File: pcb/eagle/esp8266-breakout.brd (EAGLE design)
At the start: 23.4 x 40 mm, 12 parts, among them IC1 ESP-12E/F, X1 JST-XH-11-PIN-ROUND-PAD, X2 JST-XH-11-PIN-ROUND-PAD

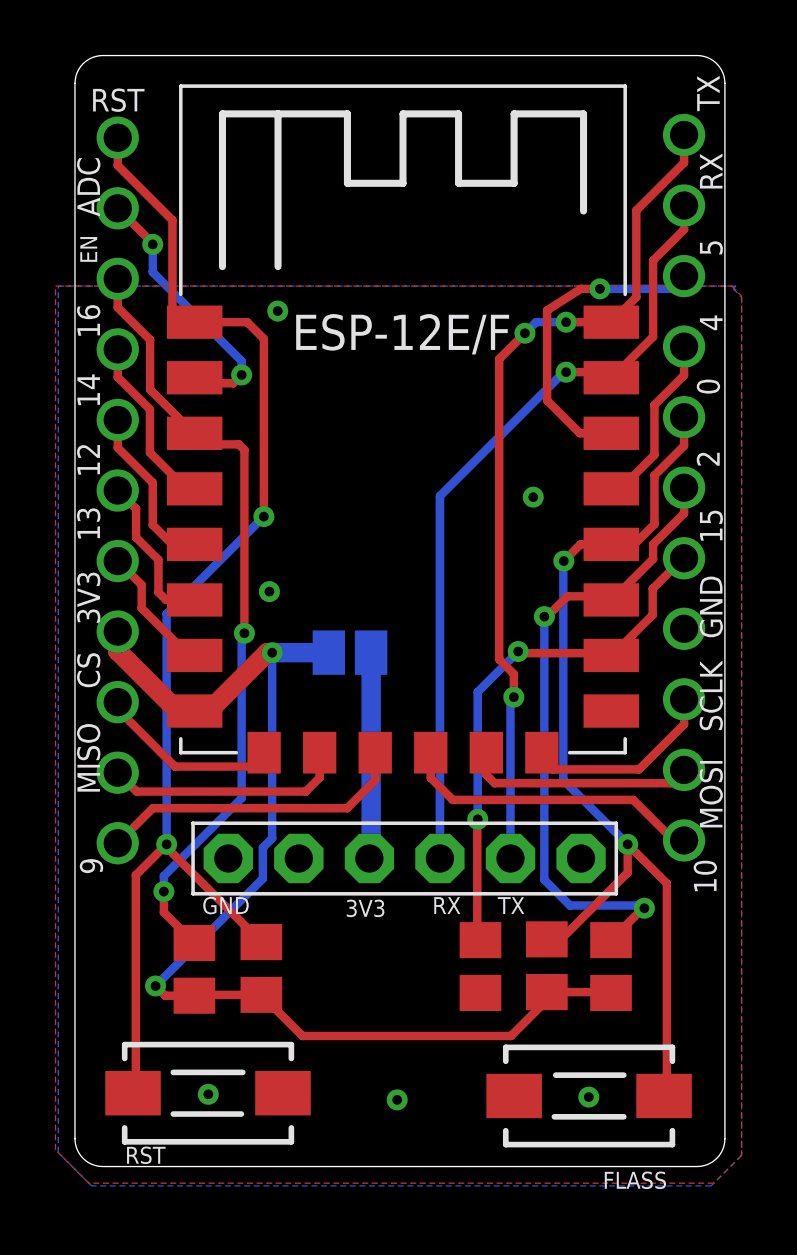
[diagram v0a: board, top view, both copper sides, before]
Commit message: Remove BUs, Rev 1.1 Completed (TODO recheck)
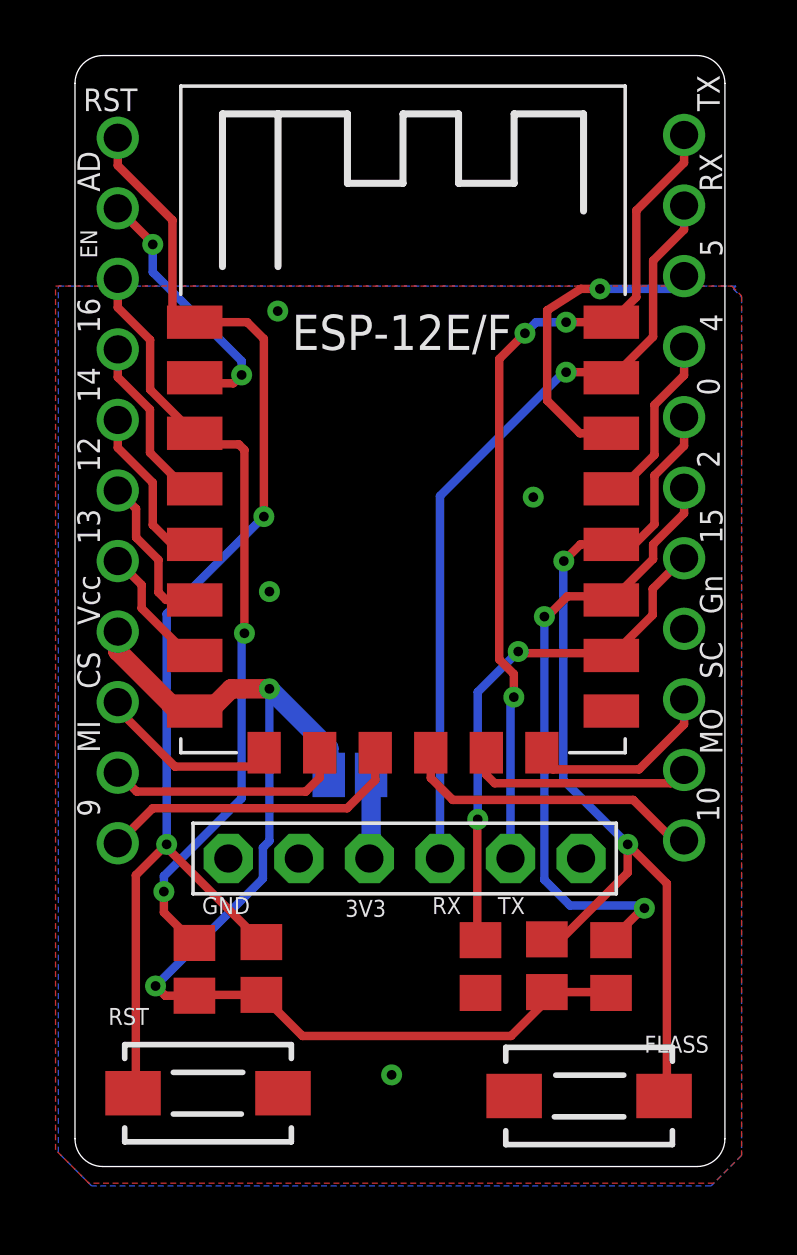
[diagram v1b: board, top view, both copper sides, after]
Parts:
- moved SJ1 4.40 mm to (9.90, 14.1)
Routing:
- net N$1: track 7.44 -> 3.04 mm
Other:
- board text added: "AD"
- board text added: "Gn"
- board text added: "MI"
- board text added: "MO"
- board text added: "SC"
- board text added: "Vcc"
- board text removed: "ADC"
- board text removed: "MISO"
- board text removed: "MOSI"
- board text removed: "SCLK"
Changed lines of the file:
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@@
 <wire x1="23.4" y1="1" x2="23.4" y2="39" width="0" layer="20"/>
 <wire x1="22.4" y1="40" x2="1" y2="40" width="0" layer="20"/>
-<text x="1.8" y="0.1" size="0.6096" layer="21">RST</text>
-<text x="19" y="-0.8" size="0.6096" layer="21">FLASS
+<text x="1.2" y="5.1" size="0.6096" layer="21">RST</text>
+<text x="20.5" y="4.1" size="0.6096" layer="21">FLASS
 </text>
 <text x="16.2" y="9.7" size="0.6096" layer="21" rot="R180">TX</text>
@@
 <text x="11.2" y="9.6" size="0.6096" layer="21" rot="R180">3V3</text>
 <text x="6.3" y="9.7" size="0.6096" layer="21" rot="R180">GND</text>
-<text x="2.5" y="38.8" size="0.8128" layer="21" rot="R180">RST</text>
-<text x="0.9" y="34.2" size="0.8128" layer="21" rot="R90">ADC</text>
-<text x="0.8" y="32.5" size="0.6096" layer="21" rot="R90">EN</text>
-<text x="0.9" y="29.8" size="0.8128" layer="21" rot="R90">16</text>
-<text x="0.9" y="27.3" size="0.8128" layer="21" rot="R90">14</text>
-<text x="0.9" y="24.8" size="0.8128" layer="21" rot="R90">12</text>
-<text x="0.9" y="22.5" size="0.8128" layer="21" rot="R90">13</text>
-<text x="0.9" y="19.5" size="0.8128" layer="21" rot="R90">3V3</text>
+<text x="0.3" y="38" size="0.8128" layer="21">RST</text>
+<text x="0.9" y="35.1" size="0.8128" layer="21" rot="R90">AD</text>
+<text x="0.8" y="32.7" size="0.6096" layer="21" rot="R90">EN</text>
+<text x="0.9" y="30" size="0.8128" layer="21" rot="R90">16</text>
+<text x="0.9" y="27.5" size="0.8128" layer="21" rot="R90">14</text>
+<text x="0.9" y="25" size="0.8128" layer="21" rot="R90">12</text>
+<text x="0.9" y="22.4" size="0.8128" layer="21" rot="R90">13</text>
+<text x="0.9" y="19.5" size="0.8128" layer="21" rot="R90">Vcc</text>
 <text x="0.9" y="17.2" size="0.8128" layer="21" rot="R90">CS</text>
-<text x="0.9" y="13.4" size="0.8128" layer="21" rot="R90">MISO</text>
-<text x="1" y="10.5" size="0.8128" layer="21" rot="R90">9</text>
+<text x="0.9" y="14.9" size="0.8128" layer="21" rot="R90">MI</text>
+<text x="0.9" y="12.6" size="0.8128" layer="21" rot="R90">9</text>
 <text x="22.4" y="39.3" size="0.8128" layer="21" rot="R270">TX</text>
-<text x="22.5" y="36.5" size="0.8128" layer="21" rot="R270">RX</text>
+<text x="23.3" y="35.1" size="0.8128" layer="21" rot="R90">RX</text>
 <text x="22.5" y="33.4" size="0.8128" layer="21" rot="R270">5</text>
 <text x="22.5" y="30.7" size="0.8128" layer="21" rot="R270">4</text>
@@
 <text x="22.4" y="25.8" size="0.8128" layer="21" rot="R270">2</text>
 <text x="22.5" y="23.7" size="0.8128" layer="21" rot="R270">15</text>
-<text x="22.5" y="21.3" size="0.8128" layer="21" rot="R270">GND</text>
-<text x="22.5" y="18.2" size="0.8128" layer="21" rot="R270">SCLK</text>
-<text x="22.5" y="14.7" size="0.8128" layer="21" rot="R270">MOSI</text>
-<text x="23.1" y="9.8" size="0.8128" layer="21" rot="R90">10</text>
-<text x="4.7" y="1.5" size="1.4224" layer="26" rot="MR180">R- 10KΩ/0805</text>
-<text x="11.3" y="16.9" size="1.4224" layer="26" rot="MR90">github.com/CSpyridak
+<text x="22.5" y="21.3" size="0.8128" layer="21" rot="R270">Gn</text>
+<text x="22.5" y="18.9" size="0.8128" layer="21" rot="R270">SC</text>
+<text x="22.5" y="16.5" size="0.8128" layer="21" rot="R270">MO</text>
+<text x="23.2" y="12.4" size="0.8128" layer="21" rot="R90">10</text>
+<text x="5.3" y="2.4" size="1.4224" layer="26" rot="MR180">R- 10KΩ/0805</text>
+<text x="10" y="16.7" size="1.4224" layer="26" rot="MR90">github.com/CSpyridak
 is/ESP8266-Breakout</text>
-<text x="8.4" y="16.7" size="1.4224" layer="26" rot="MR90">Rev.1.1 (C) 2020</text>
+<text x="19.7" y="6.6" size="1.4224" layer="26" rot="MR0">Rev.1.1 (C) 2020</text>
 <wire x1="0" y1="39" x2="0" y2="1" width="0" layer="20"/>
 <wire x1="0" y1="39" x2="1" y2="40" width="0.000009375" layer="20" curve="-90"/>
@@
 <attribute name="SPICEPREFIX" value="R" x="4.3" y="7.1" size="1.778" layer="27" rot="R90" display="off"/>
 </element>
-<element name="SJ1" library="jumper" library_urn="urn:adsk.eagle:library:252" package="SJ" package3d_urn="urn:adsk.eagle:package:15471/1" value="" x="9.9" y="18.5" smashed="yes" rot="MR180">
-<attribute name="POPULARITY" value="33" x="9.9" y="18.5" size="1.778" layer="28" rot="MR180" display="off"/>
-<attribute name="VALUE" x="10.3001" y="18.5" size="0.02" layer="28" rot="MR180"/>
+<element name="SJ1" library="jumper" library_urn="urn:adsk.eagle:library:252" package="SJ" package3d_urn="urn:adsk.eagle:package:15471/1" value="" x="9.9" y="14.1" smashed="yes" rot="MR180">
+<attribute name="POPULARITY" value="33" x="9.9" y="14.1" size="1.778" layer="28" rot="MR180" display="off"/>
+<attribute name="VALUE" x="10.3001" y="14.1" size="0.02" layer="28" rot="MR180"/>
 </element>
 </elements>
@@
 <vertex x="-0.6" y="0.5"/>
 </polygon>
-<via x="11.6" y="2.4" extent="1-16" drill="0.35" shape="octagon"/>
-<via x="18.5" y="2.5" extent="1-16" drill="0.35" shape="octagon"/>
+<via x="11.4" y="3.3" extent="1-16" drill="0.35" shape="octagon"/>
 <contactref element="R3" pad="2"/>
 <via x="16.5" y="24.1" extent="1-16" drill="0.35" shape="octagon"/>
 <via x="7" y="20.7" extent="1-16" drill="0.35" shape="octagon"/>
-<via x="4.8" y="2.6" extent="1-16" drill="0.35" shape="octagon"/>
 <via x="7.3" y="30.8" extent="1-16" drill="0.35" shape="octagon"/>
 </signal>
@@
 <contactref element="X1" pad="4"/>
 <contactref element="IC1" pad="VCC"/>
-<via x="7.1" y="18.5" extent="1-16" drill="0.35"/>
-<wire x1="7.1" y1="18.5" x2="9.138" y2="18.5" width="0.7" layer="16"/>
-<wire x1="6.9205" y1="18.5" x2="7.1" y2="18.5" width="0.7" layer="1"/>
+<via x="7" y="17.2" extent="1-16" drill="0.35"/>
+<wire x1="7" y1="17.2" x2="9.138" y2="15.062" width="0.7" layer="16"/>
+<wire x1="9.138" y1="15.062" x2="9.138" y2="14.1" width="0.7" layer="16"/>
+<wire x1="5.6205" y1="17.2" x2="7" y2="17.2" width="0.7" layer="1"/>
 <wire x1="4.3" y1="6.15" x2="4.33" y2="6.18" width="0.3048" layer="1"/>
 <wire x1="4.33" y1="6.18" x2="6.71" y2="6.18" width="0.3048" layer="1"/>
@@
 <wire x1="3.25" y1="6.15" x2="2.9" y2="6.5" width="0.3048" layer="1"/>
 <via x="2.9" y="6.5" extent="1-16" drill="0.35"/>
-<wire x1="6.7662" y1="11.48449375" x2="7.1" y2="11.81829375" width="0.3048" layer="16"/>
-<wire x1="7.1" y1="11.81829375" x2="7.1" y2="18.5" width="0.3048" layer="16"/>
+<wire x1="6.7662" y1="11.48449375" x2="7" y2="11.71829375" width="0.3048" layer="16"/>
+<wire x1="7" y1="11.71829375" x2="7" y2="17.2" width="0.3048" layer="16"/>
 <wire x1="2.9" y1="6.5" x2="6.7662" y2="10.3662" width="0.3048" layer="16"/>
 <wire x1="6.7662" y1="10.3662" x2="6.7662" y2="11.48449375" width="0.3048" layer="16"/>
@@
 <wire x1="4.3076" y1="16.3976" x2="3.7019" y2="16.3976" width="0.7" layer="1"/>
 <wire x1="4.31" y1="16.4" x2="4.8205" y2="16.4" width="0.7" layer="1"/>
-<wire x1="6.9205" y1="18.5" x2="4.8205" y2="16.4" width="0.7" layer="1"/>
+<wire x1="5.6205" y1="17.2" x2="4.8205" y2="16.4" width="0.7" layer="1"/>
 </signal>
 <signal name="N$1">
 <contactref element="SJ1" pad="2"/>
 <contactref element="JP1" pad="4"/>
-<wire x1="10.662" y1="18.5" x2="10.662" y2="11.152" width="0.7" layer="16"/>
+<wire x1="10.662" y1="14.1" x2="10.662" y2="11.152" width="0.7" layer="16"/>
 <wire x1="10.662" y1="11.152" x2="10.6" y2="11.09" width="0.7" layer="16"/>
 </signal>
